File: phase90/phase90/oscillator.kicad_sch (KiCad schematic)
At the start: 20 parts, among them U1 TL071HIDBVR, U2 TL071HIDBVR, U3 AD5162BRMZ2.5, U4 RTB05W, U5 TL071HIDBVR, U6 TL071HIDBVR

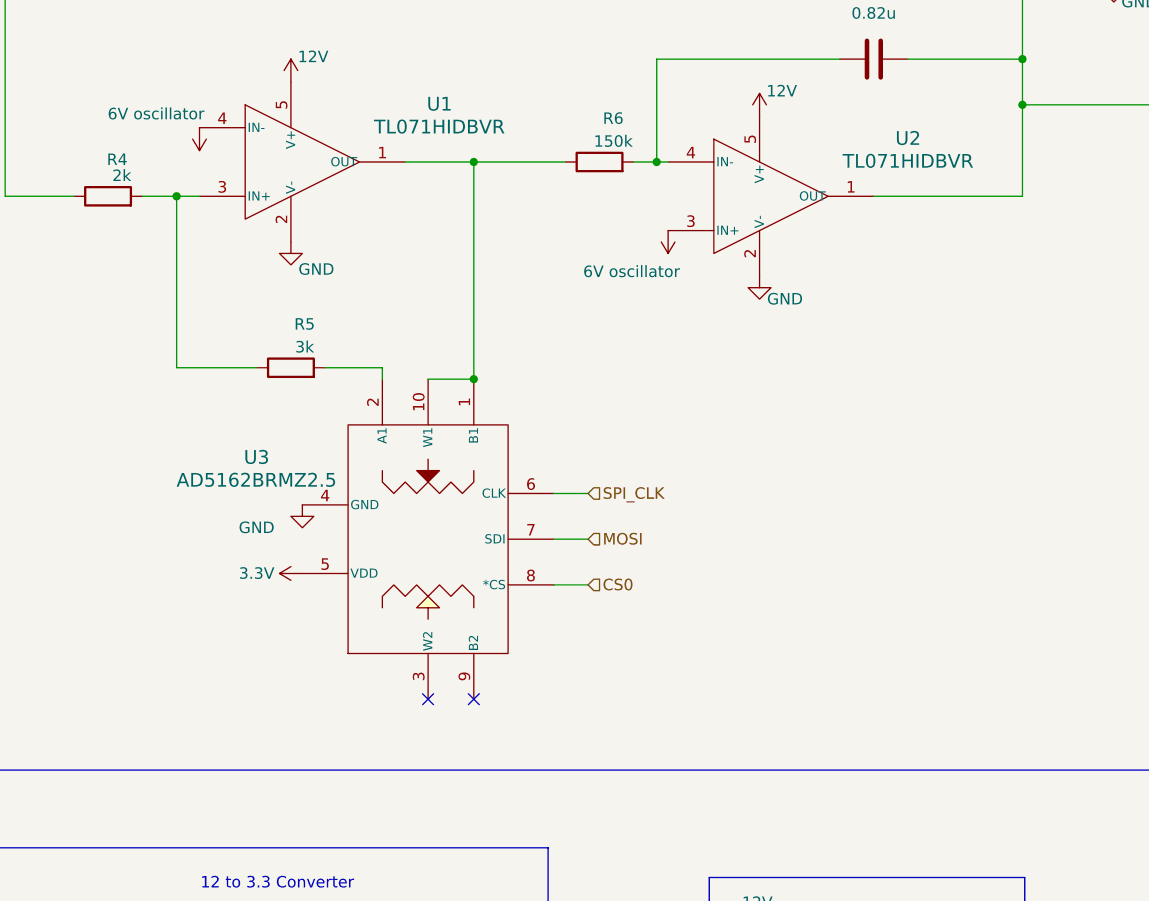
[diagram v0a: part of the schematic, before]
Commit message: changed out potentiometer for one that can do higher analog voltages
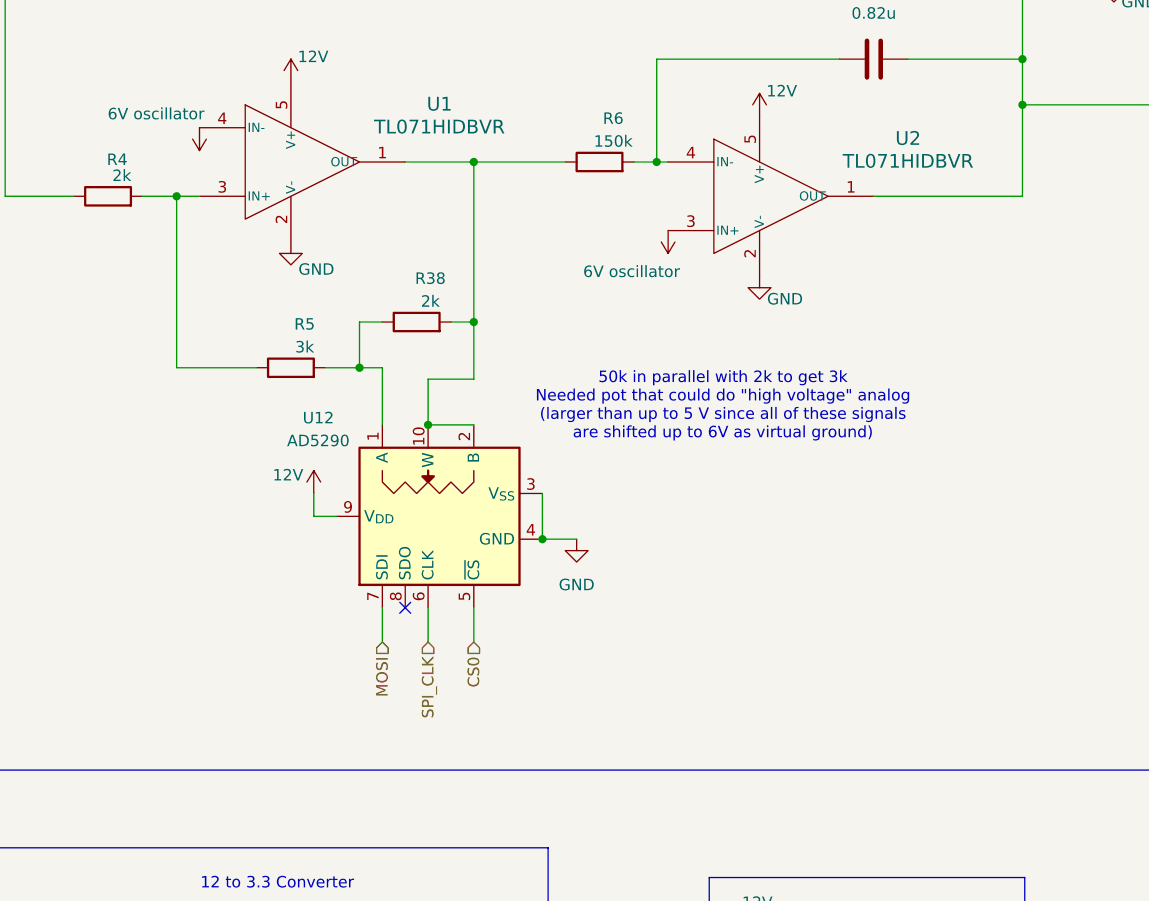
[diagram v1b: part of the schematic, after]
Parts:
- removed U3: AD5162BRMZ2.5, RM_10_ADI, symbol AD5162BRMZ2-5:AD5162BRMZ2.5
- added R38: 2k, Resistor_SMD:R_0603_1608Metric, symbol Device:R
- added U12: AD5290, Package_SO:MSOP-10_3x3mm_P0.5mm, symbol Potentiometer_Digital:AD5290
- U1, U2, U5, U6: footprint SOT23_DBV_5_TEX -> Package_TO_SOT_SMD:SOT-23-5
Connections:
- net 12V: now also U12.9 (V_{DD})
- net CS0: now also U12.5 (~{CS})
- net GND: now also U12.3 (V_{SS}), U12.4 (GND)
- net MOSI: now also U12.7 (SDI)
- net SPI_CLK: now also U12.6 (CLK)
- net at R6.1, U1.1 (OUT): now also R38.2, U12.10 (W), U12.2 (B)
- net at R5.2: now also R38.1, U12.1 (A)
- no-connect marks 2 -> 1
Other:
- note added: "50k in parallel with 2k to get 3k Needed pot that could do "high voltage" analog (larger than up to 5 V since all of these signals are shifted up to 6V as virtual ground)"

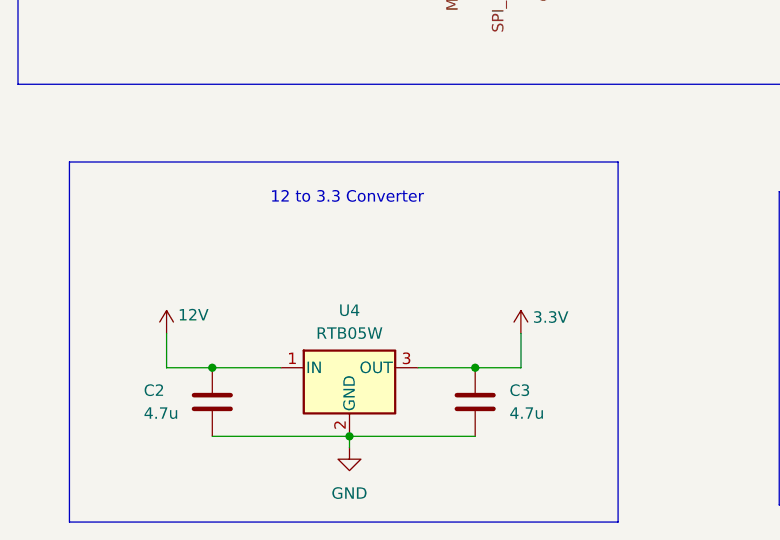
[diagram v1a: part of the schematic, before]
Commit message: updated phase 90 to not need 12 to 3 converted
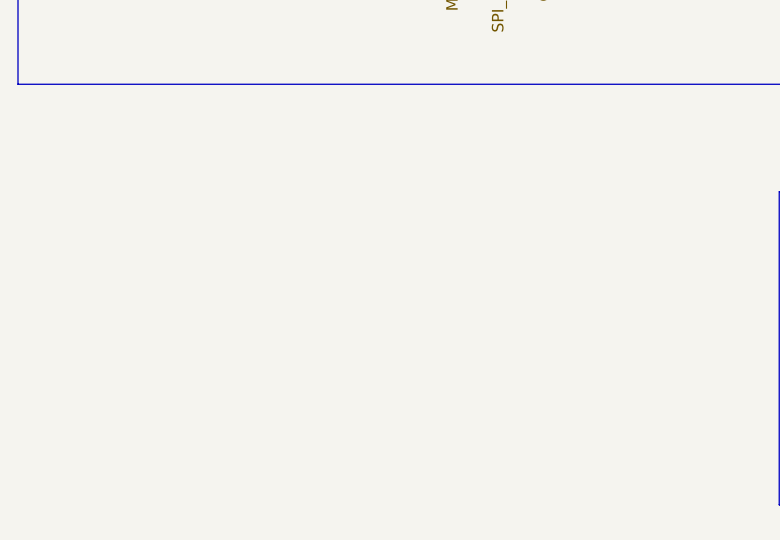
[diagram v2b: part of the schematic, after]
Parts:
- removed C2, C3: 4.7u, Capacitor_SMD:C_0603_1608Metric_Pad1.08x0.95mm_HandSolder, symbol Device:C
- removed U4: RTB05W, Converter_DCDC:Converter_DCDC_RECOM_R-78B-2.0_THT, symbol Regulator_Switching:R-78B1.5-2.0
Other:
- note removed: "12 to 3.3 Converter"

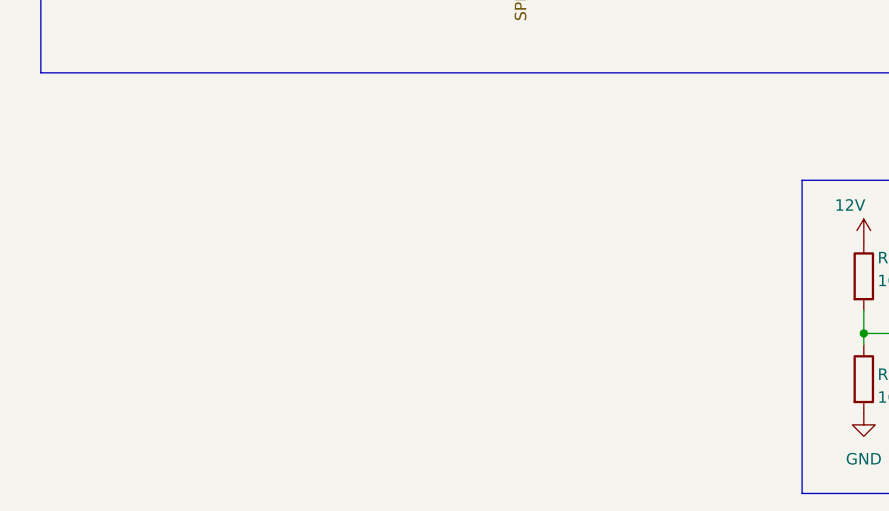
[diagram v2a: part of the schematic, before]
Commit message: added buffers and caps for op-amps on effect boards
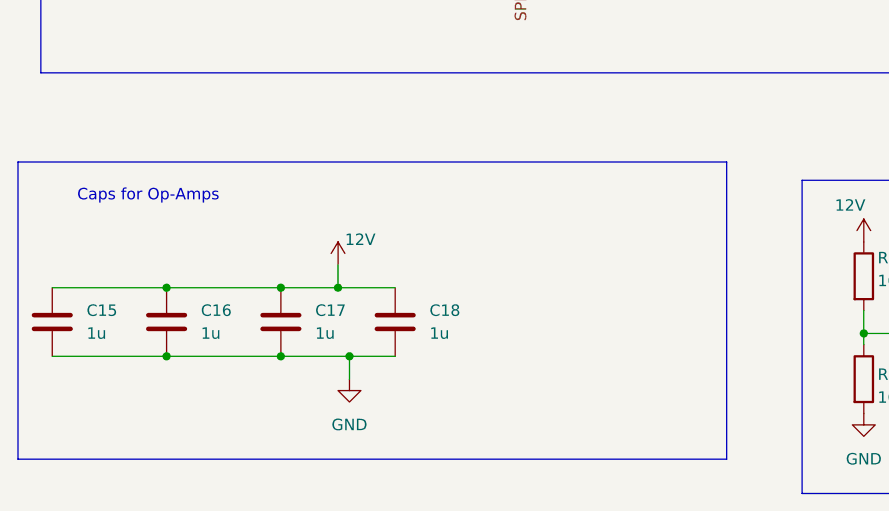
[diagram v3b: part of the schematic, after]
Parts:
- added C15, C16, C17, C18: 1u, Capacitor_SMD:C_0603_1608Metric, symbol Device:C
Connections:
- net 12V: now also C15.1, C16.1, C17.1, C18.1
- net GND: now also C15.2, C16.2, C17.2, C18.2
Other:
- note added: "Caps for Op-Amps"
